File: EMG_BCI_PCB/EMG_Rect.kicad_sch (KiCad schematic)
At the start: 25 parts, among them U3 ADA4807-4ARUZ, U8 MCP1501-18xCH

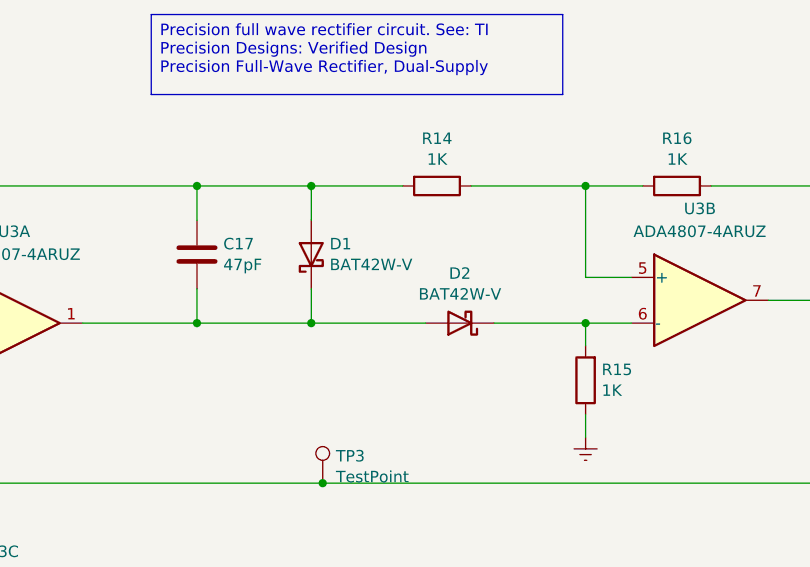
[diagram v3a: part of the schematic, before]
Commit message: Assigned footprints to components
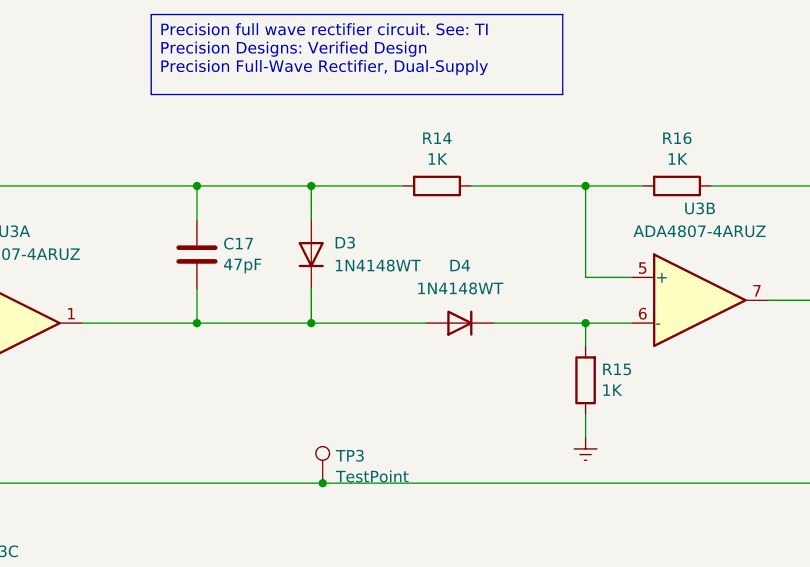
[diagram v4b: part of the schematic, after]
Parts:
- removed D1, D2: BAT42W-V, Diode_SMD:D_SOD-123, symbol EMG_Circuit:BAT42W-V
- added D3, D4: 1N4148WT, Diode_SMD:D_SOD-523, symbol Diode:1N4148WT
- C17, C18, C19, C20, C21, C22, C5, C7: footprint Capacitor_SMD:C_0603_1608Metric_Pad1.05x0.95mm_HandSolder -> Capacitor_SMD:C_0201_0603Metric_Pad0.64x0.40mm_HandSolder
- R13, R14, R15, R16, R17, R4, R5, R6: footprint Resistor_SMD:R_0805_2012Metric_Pad1.15x1.40mm_HandSolder -> Resistor_SMD:R_0603_1608Metric_Pad0.98x0.95mm_HandSolder
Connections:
- net at C17.2, U3.1: now also D3.1 (K), D4.2 (A)
- net at C17.1, R14.2, U3.3 (+): now also D3.2 (A)
- net at R15.2, U3.6 (-): now also D4.1 (K)
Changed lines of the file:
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@@
 			)
 		)
-		(property "Footprint" "Capacitor_SMD:C_0603_1608Metric_Pad1.05x0.95mm_HandSolder"
+		(property "Footprint" "Capacitor_SMD:C_0201_0603Metric_Pad0.64x0.40mm_HandSolder"
 			(at 169.8752 99.06 0)
 			(effects
@@
 			)
 		)
-		(property "Footprint" "Resistor_SMD:R_0805_2012Metric_Pad1.15x1.40mm_HandSolder"
+		(property "Footprint" "Resistor_SMD:R_0603_1608Metric_Pad0.98x0.95mm_HandSolder"
 			(at 111.252 106.68 90)
 			(effects
@@
 			)
 		)
-		(property "Footprint" "Resistor_SMD:R_0805_2012Metric_Pad1.15x1.40mm_HandSolder"
+		(property "Footprint" "Resistor_SMD:R_0603_1608Metric_Pad0.98x0.95mm_HandSolder"
 			(at 156.21 85.852 90)
 			(effects
@@
 	)
 	(symbol
-		(lib_id "EMG_Circuit:BAT42W-V")
-		(at 129.54 44.45 90)
-		(unit 1)
-		(exclude_from_sim no)
-		(in_bom yes)
-		(on_board yes)
-		(dnp no)
-		(property "Reference" "D1"
-			(at 131.572 43.2816 90)
-			(effects
-				(font
-					(size 1.27 1.27)
-				)
-				(justify right)
-			)
-		)
-		(property "Value" "BAT42W-V"
-			(at 131.572 45.593 90)
-			(effects
-				(font
-					(size 1.27 1.27)
-				)
-				(justify right)
-			)
-		)
-		(property "Footprint" "Diode_SMD:D_SOD-123"
-			(at 133.985 44.45 0)
-			(effects
-				(font
-					(size 1.27 1.27)
-				)
-				(hide yes)
-			)
-		)
-		(property "Datasheet" "http://www.vishay.com/docs/85660/bat42.pdf"
-			(at 129.54 44.45 0)
-			(effects
-				(font
-					(size 1.27 1.27)
-				)
-				(hide yes)
-			)
-		)
-		(property "Description" ""
-			(at 129.54 44.45 0)
-			(effects
-				(font
-					(size 1.27 1.27)
-				)
-			)
-		)
-		(pin "1"
-		)
-		(pin "2"
-		)
-		(instances
-			(project "EMG_BCI_PCB"
-				(path "/55cf2478-b5ba-45ce-afa6-3f75a1bb5fb4/00000000-0000-0000-0000-00005f16ee03"
-					(reference "D1")
-					(unit 1)
-				)
-			)
-		)
-	)
-	(symbol
-		(lib_id "EMG_Circuit:BAT42W-V")
-		(at 146.05 52.07 180)
-		(unit 1)
-		(exclude_from_sim no)
-		(in_bom yes)
-		(on_board yes)
-		(dnp no)
-		(property "Reference" "D2"
-			(at 146.05 46.5582 0)
-			(effects
-				(font
-					(size 1.27 1.27)
-				)
-			)
-		)
-		(property "Value" "BAT42W-V"
-			(at 146.05 48.8696 0)
-			(effects
-				(font
-					(size 1.27 1.27)
-				)
-			)
-		)
-		(property "Footprint" "Diode_SMD:D_SOD-123"
-			(at 146.05 47.625 0)
-			(effects
-				(font
-					(size 1.27 1.27)
-				)
-				(hide yes)
-			)
-		)
-		(property "Datasheet" "http://www.vishay.com/docs/85660/bat42.pdf"
-			(at 146.05 52.07 0)
-			(effects
-				(font
-					(size 1.27 1.27)
-				)
-				(hide yes)
-			)
-		)
-		(property "Description" ""
-			(at 146.05 52.07 0)
-			(effects
-				(font
-					(size 1.27 1.27)
-				)
-			)
-		)
-		(pin "1"
-		)
-		(pin "2"
-		)
-		(instances
-			(project "EMG_BCI_PCB"
-				(path "/55cf2478-b5ba-45ce-afa6-3f75a1bb5fb4/00000000-0000-0000-0000-00005f16ee03"
-					(reference "D2")
-					(unit 1)
-				)
-			)
-		)
-	)
-	(symbol
 		(lib_id "Device:C")
 		(at 116.84 44.45 0)
@@
 			)
 		)
-		(property "Footprint" "Capacitor_SMD:C_0603_1608Metric_Pad1.05x0.95mm_HandSolder"
+		(property "Footprint" "Capacitor_SMD:C_0201_0603Metric_Pad0.64x0.40mm_HandSolder"
 			(at 117.8052 48.26 0)
 			(effects
@@
 			)
 		)
-		(property "Footprint" "Resistor_SMD:R_0805_2012Metric_Pad1.15x1.40mm_HandSolder"
+		(property "Footprint" "Resistor_SMD:R_0603_1608Metric_Pad0.98x0.95mm_HandSolder"
 			(at 143.51 35.052 90)
 			(effects
@@
 			)
 		)
-		(property "Footprint" "Resistor_SMD:R_0805_2012Metric_Pad1.15x1.40mm_HandSolder"
+		(property "Footprint" "Resistor_SMD:R_0603_1608Metric_Pad0.98x0.95mm_HandSolder"
 			(at 170.18 35.052 90)
 			(effects
@@
 			)
 		)
-		(property "Footprint" "Resistor_SMD:R_0805_2012Metric_Pad1.15x1.40mm_HandSolder"
+		(property "Footprint" "Resistor_SMD:R_0603_1608Metric_Pad0.98x0.95mm_HandSolder"
 			(at 161.798 58.42 90)
 			(effects
@@
 			)
 		)
-		(property "Footprint" "Capacitor_SMD:C_0603_1608Metric_Pad1.05x0.95mm_HandSolder"
+		(property "Footprint" "Capacitor_SMD:C_0201_0603Metric_Pad0.64x0.40mm_HandSolder"
 			(at 223.2152 67.31 0)
 			(effects
@@
 			)
 		)
-		(property "Footprint" "Capacitor_SMD:C_0603_1608Metric_Pad1.05x0.95mm_HandSolder"
+		(property "Footprint" "Capacitor_SMD:C_0201_0603Metric_Pad0.64x0.40mm_HandSolder"
 			(at 234.6452 67.31 0)
 			(effects
@@
 			)
 		)
-		(property "Footprint" "Capacitor_SMD:C_0603_1608Metric_Pad1.05x0.95mm_HandSolder"
+		(property "Footprint" "Capacitor_SMD:C_0201_0603Metric_Pad0.64x0.40mm_HandSolder"
 			(at 223.2152 38.1 0)
 			(effects
@@
 			)
 		)
-		(property "Footprint" "Capacitor_SMD:C_0603_1608Metric_Pad1.05x0.95mm_HandSolder"
+		(property "Footprint" "Capacitor_SMD:C_0201_0603Metric_Pad0.64x0.40mm_HandSolder"
 			(at 234.6452 38.1 0)
 			(effects
@@
 	)
 	(symbol
+		(lib_id "Diode:1N4148WT")
+		(at 129.54 44.45 90)
+		(unit 1)
+		(exclude_from_sim no)
+		(in_bom yes)
+		(on_board yes)
+		(dnp no)
+		(fields_autoplaced yes)
+		(property "Reference" "D3"
+			(at 132.08 43.1799 90)
+			(effects
+				(font
+					(size 1.27 1.27)
+				)
+				(justify right)
+			)
+		)
+		(property "Value" "1N4148WT"
+			(at 132.08 45.7199 90)
+			(effects
+				(font
+					(size 1.27 1.27)
+				)
+				(justify right)
+			)
+		)
+		(property "Footprint" "Diode_SMD:D_SOD-523"
+			(at 133.985 44.45 0)
+			(effects
+				(font
+					(size 1.27 1.27)
+				)
+				(hide yes)
+			)
+		)
+		(property "Datasheet" "https://www.diodes.com/assets/Datasheets/ds30396.pdf"
+			(at 129.54 44.45 0)
+			(effects
+				(font
+					(size 1.27 1.27)
+				)
+				(hide yes)
+			)
+		)
+		(property "Description" "75V 0.15A Fast switching Diode, SOD-523"
+			(at 129.54 44.45 0)
+			(effects
+				(font
+					(size 1.27 1.27)
+				)
+				(hide yes)
+			)
+		)
+		(property "Sim.Device" "D"
+			(at 129.54 44.45 0)
+			(effects
+				(font
+					(size 1.27 1.27)
+				)
+				(hide yes)
+			)
+		)
+		(property "Sim.Pins" "1=K 2=A"
+			(at 129.54 44.45 0)
+			(effects
+				(font
+					(size 1.27 1.27)
+				)
+				(hide yes)
+			)
+		)
+		(pin "2"
+		)
+		(pin "1"
+		)
+		(instances
+			(project ""
+				(path "/55cf2478-b5ba-45ce-afa6-3f75a1bb5fb4/00000000-0000-0000-0000-00005f16ee03"
+					(reference "D3")
+					(unit 1)
+				)
+			)
+		)
+	)
+	(symbol
 		(lib_id "power:-3V3")
 		(at 215.9 67.31 180)
@@
 			)
 		)
-		(property "Footprint" "Capacitor_SMD:C_0603_1608Metric_Pad1.05x0.95mm_HandSolder"
+		(property "Footprint" "Capacitor_SMD:C_0201_0603Metric_Pad0.64x0.40mm_HandSolder"
 			(at 63.8048 146.05 0)
 			(effects
@@
 			)
 		)
-		(property "Footprint" "Capacitor_SMD:C_0603_1608Metric_Pad1.05x0.95mm_HandSolder"
+		(property "Footprint" "Capacitor_SMD:C_0201_0603Metric_Pad0.64x0.40mm_HandSolder"
 			(at 24.4348 146.05 0)
 			(effects
@@
 				(path "/55cf2478-b5ba-45ce-afa6-3f75a1bb5fb4/00000000-0000-0000-0000-00005f16ee03"
 					(reference "C5")
+					(unit 1)
+				)
+			)
+		)
+	)
+	(symbol
+		(lib_id "Diode:1N4148WT")
+		(at 146.05 52.07 180)
+		(unit 1)
+		(exclude_from_sim no)
+		(in_bom yes)
+		(on_board yes)
+		(dnp no)
+		(fields_autoplaced yes)
+		(property "Reference" "D4"
+			(at 146.05 45.72 0)
+			(effects
+				(font
+					(size 1.27 1.27)
+				)
+			)
+		)
+		(property "Value" "1N4148WT"
+			(at 146.05 48.26 0)
+			(effects
+				(font
+					(size 1.27 1.27)
+				)
+			)
+		)
+		(property "Footprint" "Diode_SMD:D_SOD-523"
+			(at 146.05 47.625 0)
+			(effects
+				(font
+					(size 1.27 1.27)
+				)
+				(hide yes)
+			)
+		)
+		(property "Datasheet" "https://www.diodes.com/assets/Datasheets/ds30396.pdf"
+			(at 146.05 52.07 0)
+			(effects
+				(font
+					(size 1.27 1.27)
+				)
+				(hide yes)
+			)
+		)
+		(property "Description" "75V 0.15A Fast switching Diode, SOD-523"
+			(at 146.05 52.07 0)
+			(effects
+				(font
+					(size 1.27 1.27)
+				)
+				(hide yes)
+			)
+		)
+		(property "Sim.Device" "D"
+			(at 146.05 52.07 0)
+			(effects
+				(font
+					(size 1.27 1.27)
+				)
+				(hide yes)
+			)
+		)
+		(property "Sim.Pins" "1=K 2=A"
+			(at 146.05 52.07 0)
+			(effects
+				(font
+					(size 1.27 1.27)
+				)
+				(hide yes)
+			)
+		)
+		(pin "2"
+		)
+		(pin "1"
+		)
+		(instances
+			(project "EMG_BCI_PCB"
+				(path "/55cf2478-b5ba-45ce-afa6-3f75a1bb5fb4/00000000-0000-0000-0000-00005f16ee03"
+					(reference "D4")
 					(unit 1)
 				)
@@
 			)
 		)
-		(property "Footprint" "Resistor_SMD:R_0805_2012Metric_Pad1.15x1.40mm_HandSolder"
+		(property "Footprint" "Resistor_SMD:R_0603_1608Metric_Pad0.98x0.95mm_HandSolder"
 			(at 113.03 139.192 90)
 			(effects
@@
 			)
 		)
-		(property "Footprint" "Resistor_SMD:R_0805_2012Metric_Pad1.15x1.40mm_HandSolder"
+		(property "Footprint" "Resistor_SMD:R_0603_1608Metric_Pad0.98x0.95mm_HandSolder"
 			(at 93.98 127.762 90)
 			(effects
@@
 			)
 		)
-		(property "Footprint" "Resistor_SMD:R_0805_2012Metric_Pad1.15x1.40mm_HandSolder"
+		(property "Footprint" "Resistor_SMD:R_0603_1608Metric_Pad0.98x0.95mm_HandSolder"
 			(at 93.98 139.192 90)
 			(effects

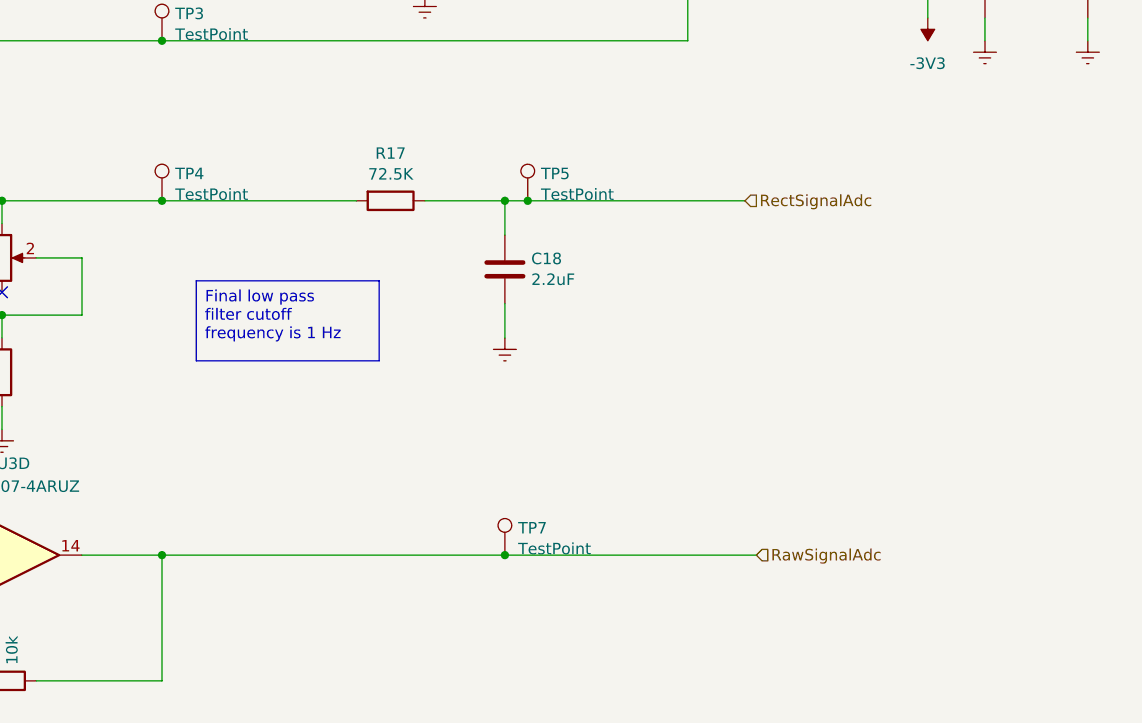
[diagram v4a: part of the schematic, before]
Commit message: finally assigned the footprints to the schematic symbols
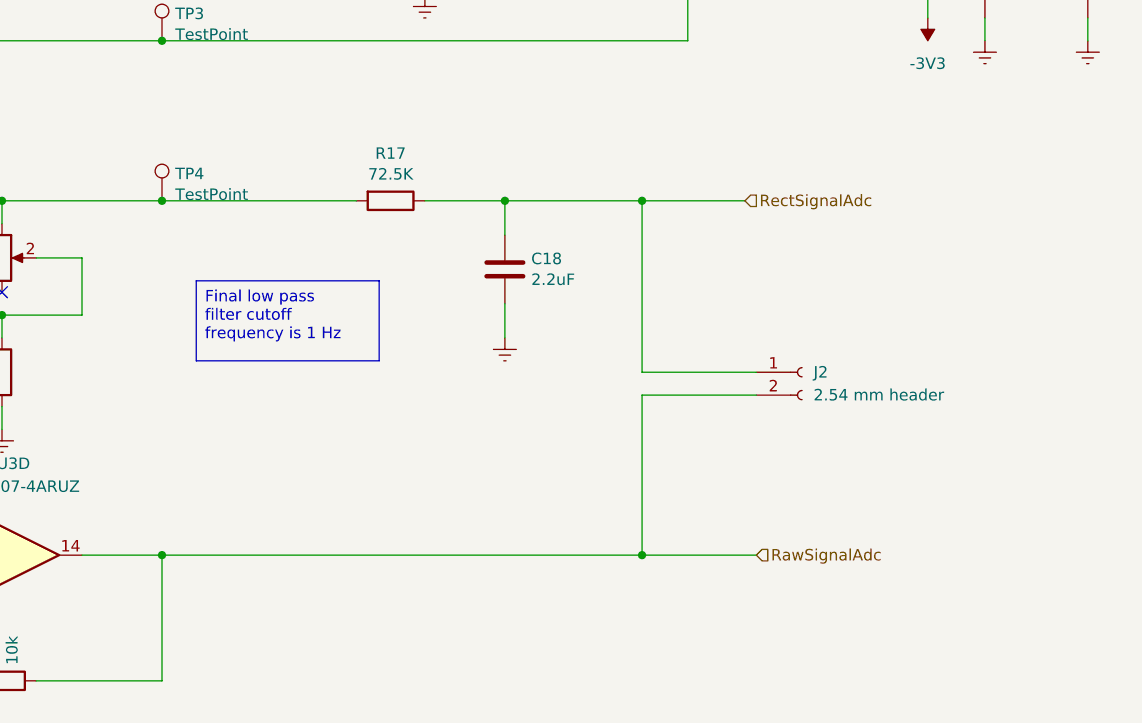
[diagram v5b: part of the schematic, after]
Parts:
- removed TP5, TP7: TestPoint, Connector_PinHeader_2.54mm:PinHeader_1x01_P2.54mm_Vertical, symbol Connector:TestPoint
- added J2: 2.54 mm header, Connector_PinSocket_2.54mm:PinSocket_1x02_P2.54mm_Vertical, symbol Connector:Conn_01x02_Socket
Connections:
- net RawSignalAdc: now also J2.2 (Pin_2)
- net RectSignalAdc: now also J2.1 (Pin_1)
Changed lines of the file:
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@@
 	)
 	(junction
-		(at 171.45 87.63)
-		(diameter 0)
-		(color 0 0 0 0)
-	)
-	(junction
 		(at 113.03 100.33)
 		(diameter 0)
@@
 	)
 	(junction
+		(at 184.15 87.63)
+		(diameter 0)
+		(color 0 0 0 0)
+	)
+	(junction
 		(at 222.25 58.42)
 		(diameter 0)
@@
 	)
 	(junction
-		(at 168.91 127)
+		(at 102.87 140.97)
 		(diameter 0)
 		(color 0 0 0 0)
 	)
 	(junction
-		(at 102.87 140.97)
+		(at 184.15 127)
 		(diameter 0)
 		(color 0 0 0 0)
@@
 	(wire
 		(pts
+			(xy 184.15 127) (xy 196.85 127)
+		)
+		(stroke
+			(width 0)
+			(type default)
+		)
+	)
+	(wire
+		(pts
 			(xy 113.03 87.63) (xy 130.81 87.63)
 		)
@@
 	(wire
 		(pts
-			(xy 222.25 58.42) (xy 215.9 58.42)
+			(xy 184.15 87.63) (xy 195.58 87.63)
 		)
 		(stroke
@@
 	(wire
 		(pts
-			(xy 171.45 87.63) (xy 195.58 87.63)
+			(xy 222.25 58.42) (xy 215.9 58.42)
 		)
 		(stroke
@@
 	(wire
 		(pts
-			(xy 160.02 52.07) (xy 149.86 52.07)
+			(xy 168.91 87.63) (xy 184.15 87.63)
 		)
 		(stroke
@@
 	(wire
 		(pts
-			(xy 233.68 29.21) (xy 222.25 29.21)
+			(xy 160.02 52.07) (xy 149.86 52.07)
 		)
 		(stroke
@@
 	(wire
 		(pts
-			(xy 233.68 58.42) (xy 222.25 58.42)
+			(xy 233.68 29.21) (xy 222.25 29.21)
 		)
 		(stroke
@@
 	(wire
 		(pts
-			(xy 69.85 54.61) (xy 88.9 54.61)
+			(xy 233.68 58.42) (xy 222.25 58.42)
 		)
 		(stroke
@@
 	(wire
 		(pts
-			(xy 25.4 153.67) (xy 25.4 156.21)
+			(xy 69.85 54.61) (xy 88.9 54.61)
 		)
 		(stroke
@@
 	(wire
 		(pts
-			(xy 130.81 140.97) (xy 130.81 127)
+			(xy 25.4 153.67) (xy 25.4 156.21)
 		)
 		(stroke
@@
 	(wire
 		(pts
-			(xy 90.17 129.54) (xy 69.85 129.54)
+			(xy 130.81 140.97) (xy 130.81 127)
 		)
 		(stroke
@@
 	(wire
 		(pts
-			(xy 168.91 127) (xy 196.85 127)
+			(xy 90.17 129.54) (xy 69.85 129.54)
 		)
 		(stroke
@@
 	(wire
 		(pts
+			(xy 184.15 106.68) (xy 184.15 87.63)
+		)
+		(stroke
+			(width 0)
+			(type default)
+		)
+	)
+	(wire
+		(pts
 			(xy 165.1 46.99) (xy 160.02 46.99)
 		)
@@
 	(wire
 		(pts
-			(xy 168.91 87.63) (xy 171.45 87.63)
+			(xy 185.42 49.53) (xy 189.23 49.53)
 		)
 		(stroke
@@
 	(wire
 		(pts
-			(xy 185.42 49.53) (xy 189.23 49.53)
+			(xy 121.92 93.98) (xy 116.84 93.98)
 		)
 		(stroke
@@
 	(wire
 		(pts
-			(xy 121.92 93.98) (xy 116.84 93.98)
+			(xy 139.7 36.83) (xy 129.54 36.83)
 		)
 		(stroke
@@
 	(wire
 		(pts
-			(xy 139.7 36.83) (xy 129.54 36.83)
+			(xy 189.23 69.85) (xy 130.81 69.85)
 		)
 		(stroke
@@
 	(wire
 		(pts
-			(xy 189.23 69.85) (xy 130.81 69.85)
+			(xy 168.91 99.06) (xy 168.91 102.87)
 		)
 		(stroke
@@
 	(wire
 		(pts
-			(xy 168.91 99.06) (xy 168.91 102.87)
+			(xy 184.15 109.22) (xy 184.15 127)
 		)
 		(stroke
@@
 	(wire
 		(pts
+			(xy 196.85 106.68) (xy 184.15 106.68)
+		)
+		(stroke
+			(width 0)
+			(type default)
+		)
+	)
+	(wire
+		(pts
 			(xy 113.03 87.63) (xy 102.87 87.63)
 		)
@@
 	(wire
 		(pts
-			(xy 130.81 127) (xy 168.91 127)
+			(xy 130.81 127) (xy 184.15 127)
 		)
 		(stroke
@@
 	(wire
 		(pts
+			(xy 196.85 109.22) (xy 184.15 109.22)
+		)
+		(stroke
+			(width 0)
+			(type default)
+		)
+	)
+	(wire
+		(pts
 			(xy 130.81 127) (xy 121.92 127)
 		)
@@
 	(symbol
 		(lib_id "Connector:TestPoint")
-		(at 171.45 87.63 0)
-		(unit 1)
-		(exclude_from_sim no)
-		(in_bom yes)
-		(on_board yes)
-		(dnp no)
-		(property "Reference" "TP5"
-			(at 172.9232 84.6328 0)
-			(effects
-				(font
-					(size 1.27 1.27)
-				)
-				(justify left)
-			)
-		)
-		(property "Value" "TestPoint"
-			(at 172.9232 86.9442 0)
-			(effects
-				(font
-					(size 1.27 1.27)
-				)
-				(justify left)
-			)
-		)
-		(property "Footprint" "Connector_PinHeader_2.54mm:PinHeader_1x01_P2.54mm_Vertical"
-			(at 176.53 87.63 0)
-			(effects
-				(font
-					(size 1.27 1.27)
-				)
-				(hide yes)
-			)
-		)
-		(property "Datasheet" "~"
-			(at 176.53 87.63 0)
-			(effects
-				(font
-					(size 1.27 1.27)
-				)
-				(hide yes)
-			)
-		)
-		(property "Description" ""
-			(at 171.45 87.63 0)
-			(effects
-				(font
-					(size 1.27 1.27)
-				)
-			)
-		)
-		(pin "1"
-		)
-		(instances
-			(project "EMG_BCI_PCB"
-				(path "/55cf2478-b5ba-45ce-afa6-3f75a1bb5fb4/00000000-0000-0000-0000-00005f16ee03"
-					(reference "TP5")
-					(unit 1)
-				)
-			)
-		)
-	)
-	(symbol
-		(lib_id "Connector:TestPoint")
 		(at 130.81 87.63 0)
 		(unit 1)
@@
 	)
 	(symbol
-		(lib_id "Connector:TestPoint")
-		(at 168.91 127 0)
+		(lib_id "power:+3.3V")
+		(at 215.9 26.67 0)
 		(unit 1)
 		(exclude_from_sim no)
@@
 		(on_board yes)
 		(dnp no)
-		(property "Reference" "TP7"
-			(at 170.3832 124.0028 0)
+		(fields_autoplaced yes)
+		(property "Reference" "#PWR041"
+			(at 215.9 30.48 0)
 			(effects
 				(font
 					(size 1.27 1.27)
 				)
-				(justify left)
+				(hide yes)
 			)
 		)
-		(property "Value" "TestPoint"
-			(at 170.3832 126.3142 0)
+		(property "Value" "+3.3V"
+			(at 215.9 21.59 0)
 			(effects
 				(font
 					(size 1.27 1.27)
 				)
-				(justify left)
 			)
 		)
-		(property "Footprint" "Connector_PinHeader_2.54mm:PinHeader_1x01_P2.54mm_Vertical"
-			(at 173.99 127 0)
+		(property "Footprint" ""
+			(at 215.9 26.67 0)
 			(effects
 				(font
@@
 			)
 		)
-		(property "Datasheet" "~"
-			(at 173.99 127 0)
+		(property "Datasheet" ""
+			(at 215.9 26.67 0)
 			(effects
 				(font
@@
 			)
 		)
-		(property "Description" ""
-			(at 168.91 127 0)
+		(property "Description" "Power symbol creates a global label with name \"+3.3V\""
+			(at 215.9 26.67 0)
 			(effects
 				(font
 					(size 1.27 1.27)
 				)
+				(hide yes)
 			)
 		)
@@
 			(project "EMG_BCI_PCB"
 				(path "/55cf2478-b5ba-45ce-afa6-3f75a1bb5fb4/00000000-0000-0000-0000-00005f16ee03"
-					(reference "TP7")
+					(reference "#PWR041")
 					(unit 1)
 				)
@@
 	)
 	(symbol
-		(lib_id "power:+3.3V")
-		(at 215.9 26.67 0)
+		(lib_id "Connector:Conn_01x02_Socket")
+		(at 201.93 106.68 0)
 		(unit 1)
 		(exclude_from_sim no)
@@
 		(dnp no)
 		(fields_autoplaced yes)
-		(property "Reference" "#PWR041"
-			(at 215.9 30.48 0)
+		(property "Reference" "J2"
+			(at 203.2 106.6799 0)
 			(effects
 				(font
 					(size 1.27 1.27)
 				)
-				(hide yes)
+				(justify left)
 			)
 		)
-		(property "Value" "+3.3V"
-			(at 215.9 21.59 0)
+		(property "Value" "2.54 mm header"
+			(at 203.2 109.2199 0)
 			(effects
 				(font
 					(size 1.27 1.27)
 				)
+				(justify left)
 			)
 		)
-		(property "Footprint" ""
-			(at 215.9 26.67 0)
+		(property "Footprint" "Connector_PinSocket_2.54mm:PinSocket_1x02_P2.54mm_Vertical"
+			(at 201.93 106.68 0)
 			(effects
 				(font
@@
 			)
 		)
-		(property "Datasheet" ""
-			(at 215.9 26.67 0)
+		(property "Datasheet" "~"
+			(at 201.93 106.68 0)
 			(effects
 				(font
@@
 			)
 		)
-		(property "Description" "Power symbol creates a global label with name \"+3.3V\""
-			(at 215.9 26.67 0)
+		(property "Description" "Generic connector, single row, 01x02, script generated"
+			(at 201.93 106.68 0)
 			(effects
 				(font
@@
 			)
 		)
+		(pin "2"
+		)
 		(pin "1"
 		)
 		(instances
-			(project "EMG_BCI_PCB"
+			(project ""
 				(path "/55cf2478-b5ba-45ce-afa6-3f75a1bb5fb4/00000000-0000-0000-0000-00005f16ee03"
-					(reference "#PWR041")
+					(reference "J2")
 					(unit 1)
 				)
